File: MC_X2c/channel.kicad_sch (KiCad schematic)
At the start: 15 parts, among them J1 Screw_Terminal_01x02, K1 Channel 1, Q1 2N3904, SW1 SW_Slide_DPDT, U2 PC817, U3 H11AA1

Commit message: Working progress - migration to MAC
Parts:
- added C22: 100nF, symbol Device:C
- added R90: 10k, symbol Device:R
- renumbered R5 to R10, R6 to R11, R7 to R12, R1 to R6, R2 to R7, R3 to R8, R4 to R9, U2 to U3, U3 to U4
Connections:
- net +5V: now also R90.2
- net GND: now also C22.2
- net RC: now also C22.1, R90.1
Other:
- title: (none) -> Channel

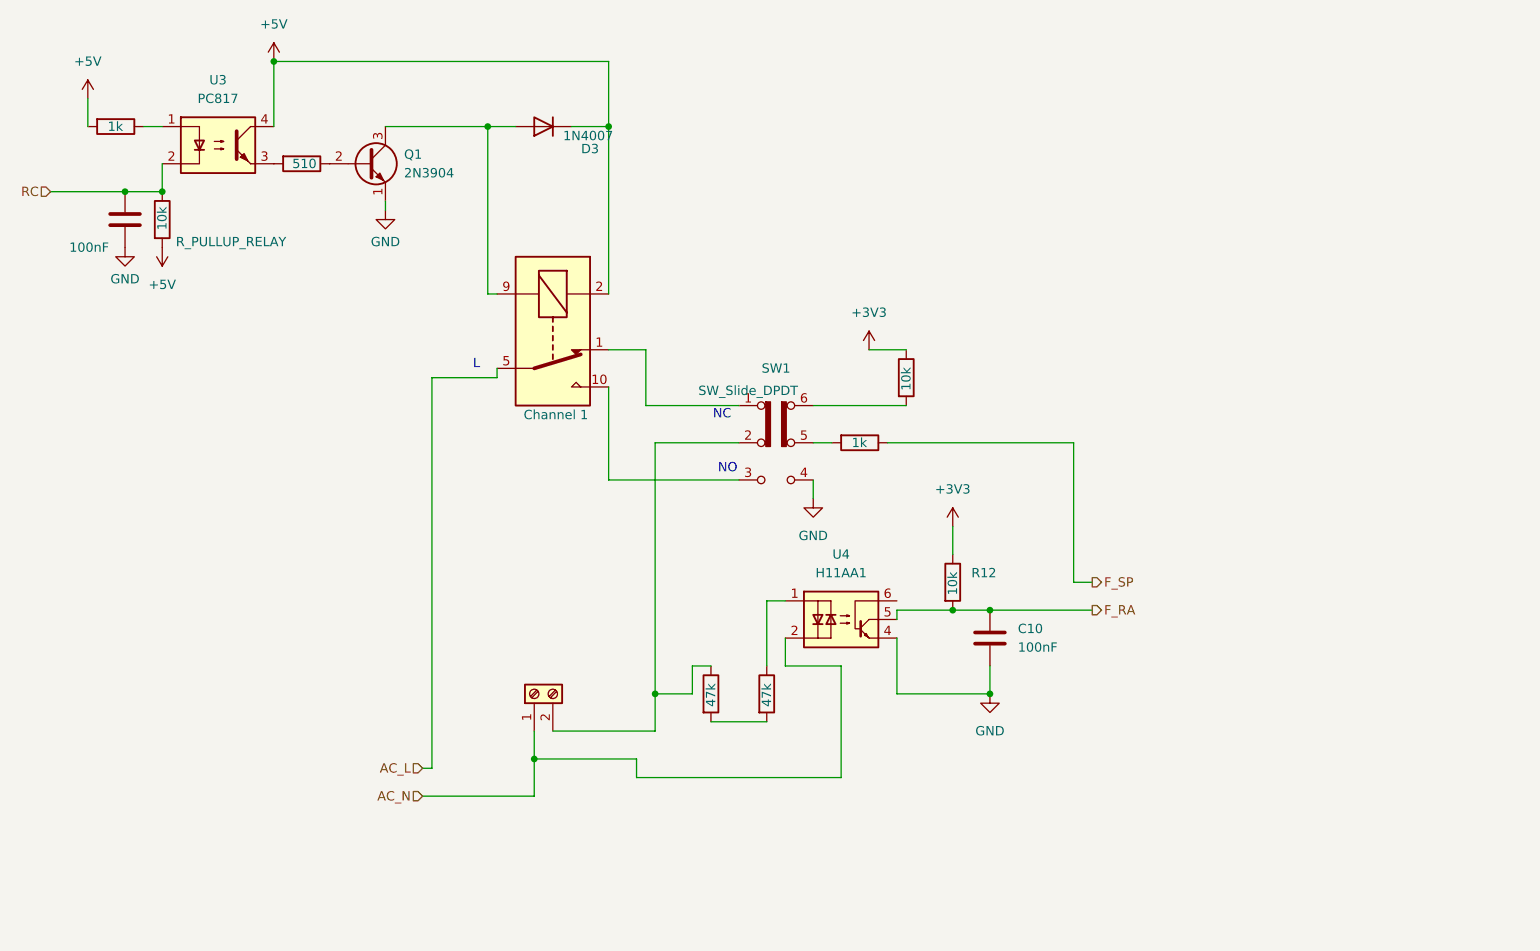
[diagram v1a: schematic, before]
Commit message: Proper namings in AC_ENTRY and CHANNEL + passives on root
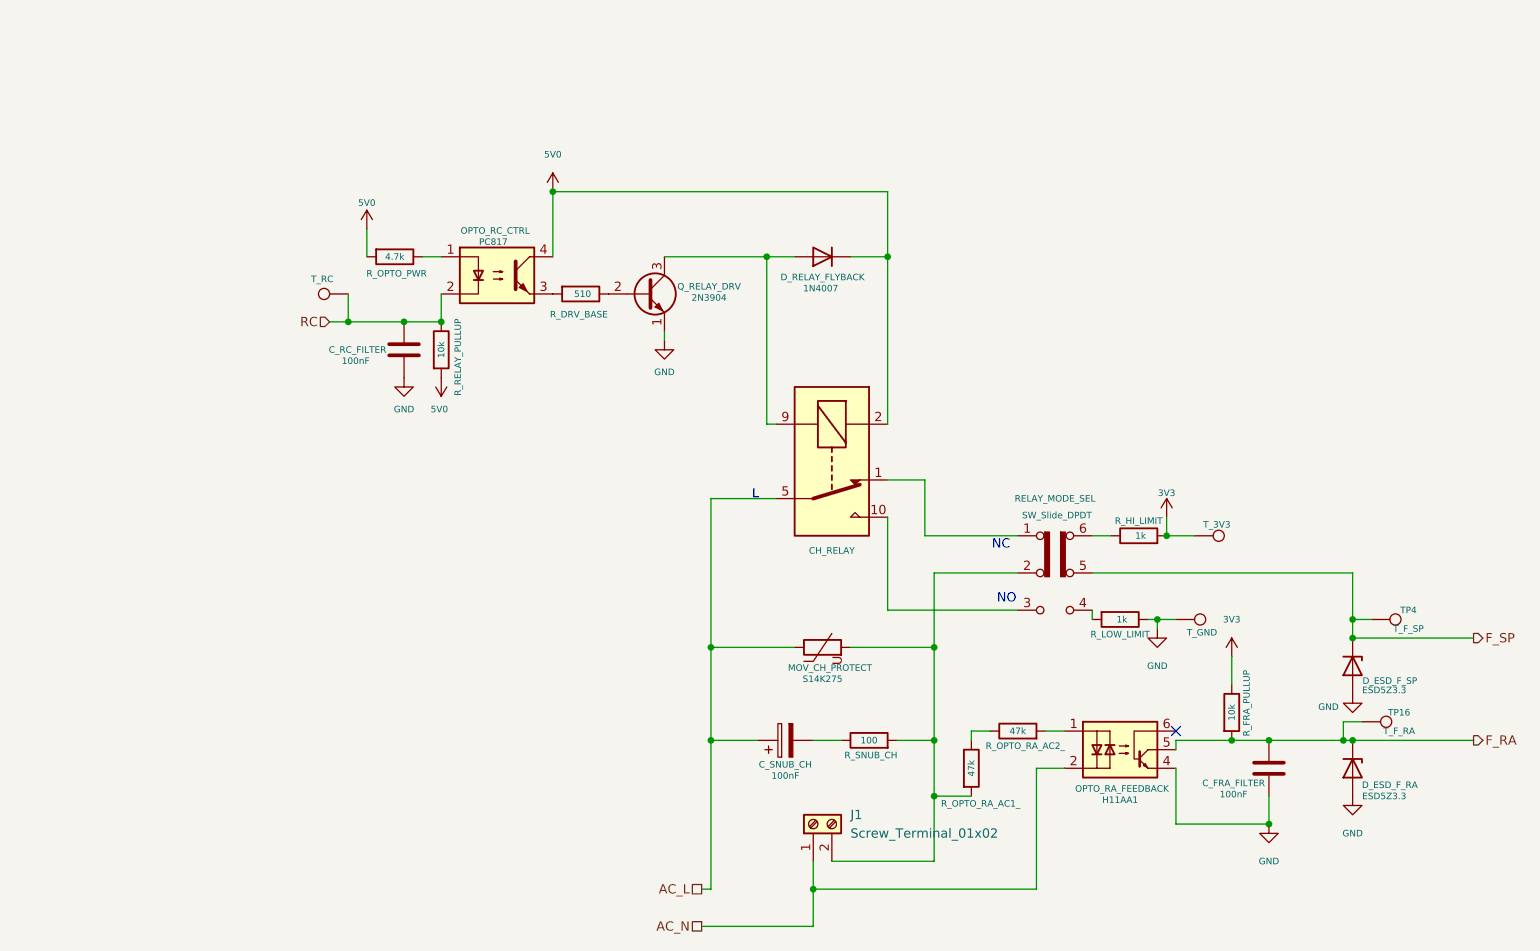
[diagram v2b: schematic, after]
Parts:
- added C_SNUB_CH: 100nF, symbol Device:C_Polarized
- added D_ESD_F_RA, D_ESD_F_SP: ESD5Z3.3, Diode_SMD:D_SOD-523, symbol Diode:ESD5Zxx
- added MOV_CH_PROTECT: S14K275, symbol Device:Varistor
- added R_SNUB_CH: 100, symbol Device:R
- added TP16: T_F_RA, symbol Connector:TestPoint
- added TP4: T_F_SP, symbol Connector:TestPoint
- added T_3V3, T_GND: T_3V3, symbol Connector:TestPoint
- added T_RC: T_RC, symbol Connector:TestPoint
- CH_RELAY: renamed from K1; value Channel 1 -> Channel
- J1: footprint nelees:1017503 -> (none)
- R_HI_LIMIT: renamed from R11; value 10k -> 1k
- R_OPTO_PWR: renamed from R6; value 1k -> 4.7k
- R_RELAY_PULLUP: renamed from R90; Info R_PULLUP_RELAY -> (none)
- renumbered C10 to C_FRA_FILTER, C22 to C_RC_FILTER, D3 to D_RELAY_FLYBACK, U4 to OPTO_RA_FEEDBACK, U3 to OPTO_RC_CTRL, Q1 to Q_RELAY_DRV, SW1 to RELAY_MODE_SEL, R7 to R_DRV_BASE, R12 to R_FRA_PULLUP, R10 to R_LOW_LIMIT, R8 to R_OPTO_RA_AC1_, R9 to R_OPTO_RA_AC2_
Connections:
- net AC_L: now also C_SNUB_CH.1, MOV_CH_PROTECT.1
- net F_RA: now also D_ESD_F_RA.1 (K), TP16.1
- net F_SP: now also RELAY_MODE_SEL.5 (B), D_ESD_F_SP.1 (K), TP4.1; no longer R_LOW_LIMIT.1
- net GND: now also R_LOW_LIMIT.1, D_ESD_F_RA.2 (A), D_ESD_F_SP.2 (A), T_GND.1; no longer RELAY_MODE_SEL.4 (A)
- net RC: now also T_RC.1
- net at OPTO_RA_FEEDBACK.1: now also R_OPTO_RA_AC2_.2; no longer R_OPTO_RA_AC2_.1
- net at J1.2 (Pin_2), RELAY_MODE_SEL.2 (B): now also R_OPTO_RA_AC1_.2, MOV_CH_PROTECT.2, R_SNUB_CH.2; no longer R_OPTO_RA_AC1_.1
- net at RELAY_MODE_SEL.6 (C): now also R_HI_LIMIT.1; no longer R_HI_LIMIT.2
- net at R_LOW_LIMIT.2: now also RELAY_MODE_SEL.4 (A); no longer RELAY_MODE_SEL.5 (B)
- net +3V3 renamed 3V3
- net 3V3: now also R_HI_LIMIT.2, T_3V3.1; no longer R_HI_LIMIT.1
- net +5V renamed 5V0
- new net: R_OPTO_RA_AC1_.1, R_OPTO_RA_AC2_.1
- new net: C_SNUB_CH.2, R_SNUB_CH.1
- no-connect marks 0 -> 1
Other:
- moved on the sheet: C_FRA_FILTER, D_RELAY_FLYBACK, OPTO_RA_FEEDBACK, OPTO_RC_CTRL, Q_RELAY_DRV, RELAY_MODE_SEL, R_FRA_PULLUP

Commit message: Fix channel refference names and add fuse for channel out
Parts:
- added F_CH1: Littelfuse 273.200, symbol Device:Fuse
- renumbered J1 to CH_OUT1, CH_RELAY to CH_RELAY1, C_FRA_FILTER to C_FRA_FILTER1, C_RC_FILTER to C_RC_FILTER1, C_SNUB_CH to C_SNUB1, D_ESD_F_RA to D_ESD_F_RA1, D_ESD_F_SP to D_ESD_F_SP1, D_RELAY_FLYBACK to D_RELAY_FLYBACK1, MOV_CH_PROTECT to MOV_CH_PROTECT1, OPTO_RA_FEEDBACK to OPTO_RA_FEEDBACK1, OPTO_RC_CTRL to OPTO_RC_CTRL1, Q_RELAY_DRV to Q_RELAY_DRV1, RELAY_MODE_SEL to RELAY_MODE_SEL1, R_DRV_BASE to R_DRV_BASE1, R_FRA_PULLUP to R_FRA_PULLUP1, R_HI_LIMIT to R_HI_LIMIT1, R_LOW_LIMIT to R_LOW_LIMIT1, R_OPTO_PWR to R_OPTO_PWR1, R_OPTO_RA_AC1_ to R_OPTO_RA_AC1_1, R_OPTO_RA_AC2_ to R_OPTO_RA_AC2_1, R_RELAY_PULLUP to R_RELAY_PULLUP1, R_SNUB_CH to R_SNUB1, T_3V3 to T_3V1, TP16 to T_F_RA_1, TP4 to T_F_SP_1, T_GND to T_GND1, T_RC to T_RC1
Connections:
- net at MOV_CH_PROTECT1.2, RELAY_MODE_SEL1.2 (B), R_OPTO_RA_AC1_1.2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: now also F_CH1.2; no longer CH_OUT1.2 (Pin_2)
- new net: CH_OUT1.2 (Pin_2), F_CH1.1
